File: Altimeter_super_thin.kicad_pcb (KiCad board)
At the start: 4 copper layers, 54.5 x 18 mm, 104 parts, among them IC1 XTSD02GLGEAG, J1 Conn_01x04_Male, J2 Conn_01x02_Male, J3 USB_C_Receptacle_USB2.0, J4 Conn_01x02_Male, Q1 PMV20ENR, U1 150044M155220, U10 MAX77827AEFD+T, U11 SC4215, U2 ESP32-S3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

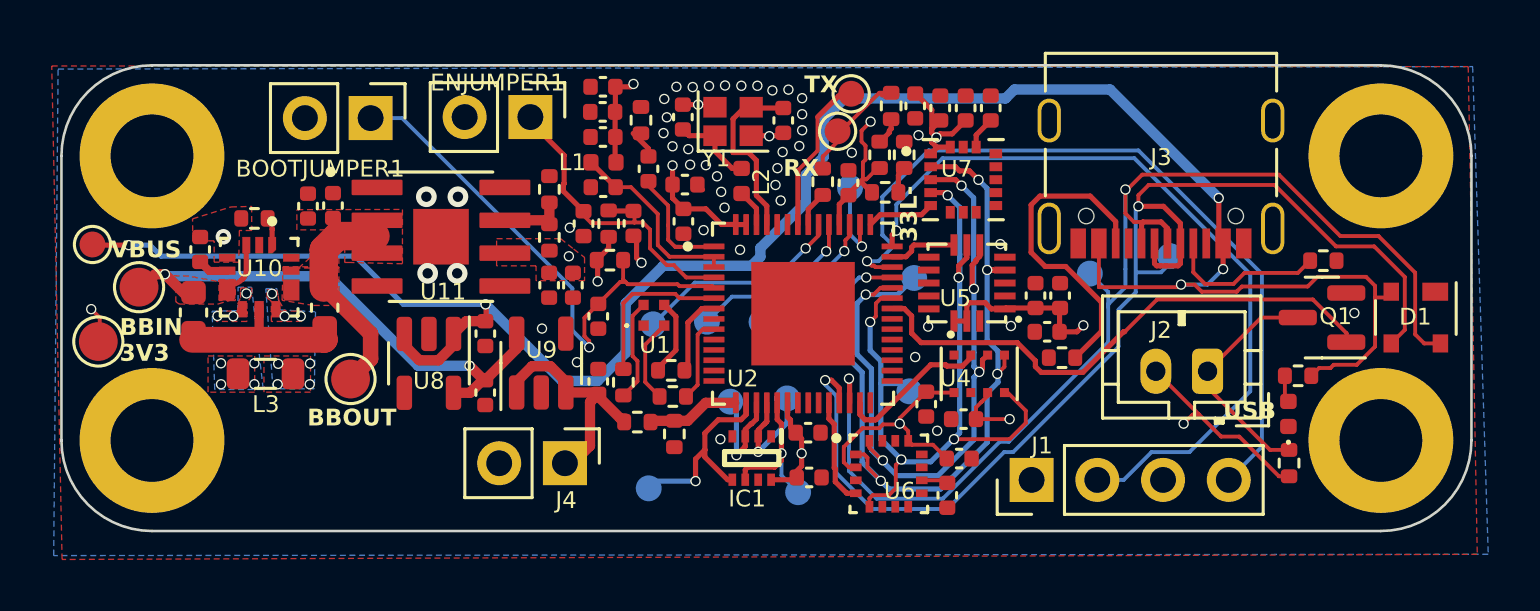
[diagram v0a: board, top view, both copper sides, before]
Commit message: spaced out vias and changed j4
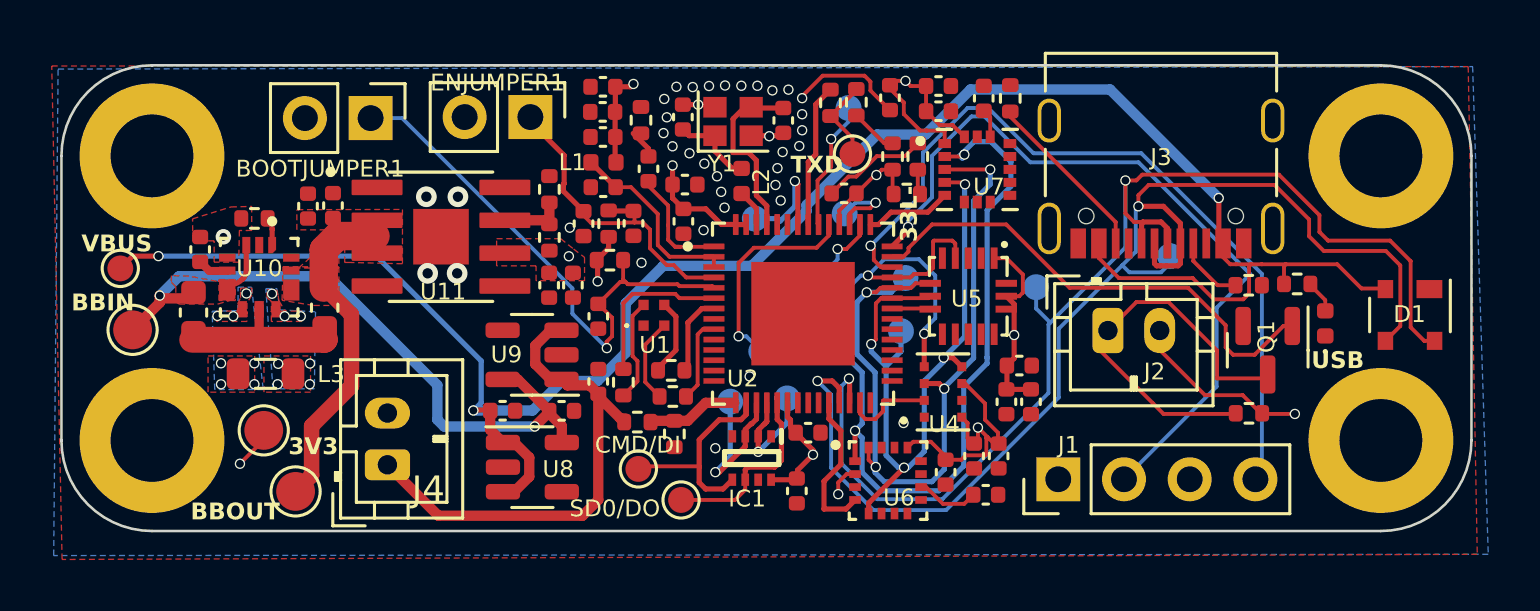
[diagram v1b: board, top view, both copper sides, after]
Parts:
- J4: footprint Connector_PinHeader_2.54mm:PinHeader_1x02_P2.54mm_Vertical -> Connector_JST:JST_PH_B2B-PH-K_1x02_P2.00mm_Vertical
- TP14, TP7: moved to F.Cu
- TP2: moved to B.Cu
- moved TP19 11.3 mm to (113.4, 86.7)
- moved R13 10.2 mm to (119.7, 86.3), turned to -90 degrees
- moved TP9 7.26 mm to (90.8, 99.1), turned to 180 degrees
- moved J4 6.86 mm to (95.6, 100.4), turned to 90 degrees
- moved TP2 6.10 mm to (109.8, 90.9), turned to 180 degrees
- moved U8 5.66 mm to (101.2, 100.5), turned to 0 degrees
- moved TP17 5.29 mm to (113.3, 90.7)
- moved TP8 4.84 mm to (92.0, 101.5)
- moved C39 4.60 mm to (119.5, 98.0), turned to 90 degrees
- moved TP14 4.53 mm to (107.0, 101.8), turned to 0 degrees
- moved J2 4.16 mm to (123.5, 95.2), turned to 0 degrees
- moved C18 4.11 mm to (120.5, 98.0), turned to 90 degrees
- moved TP16 3.95 mm to (112.1, 93.4)
- moved USBLED1 3.78 mm to (131.8, 95.0)
- moved R14 3.55 mm to (130.8, 93.5), turned to 0 degrees
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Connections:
- U2 pad 36: /Buzzer -> /Accel
- U2 pad 41: /IMU/Accelerometer -> /Buzzer
- U5 pad 8: /IMU/Accelerometer -> /Accel
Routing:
- net /SCLK: track 32.0 -> 44.9 mm, vias 5 -> 4
- net Net-(J4-Pin_1): track 9.55 -> 19.7 mm
- net GND: track 10.2 -> 17.5 mm, vias 48 -> 38
- net VBUS: track 84.5 -> 78.4 mm, vias 5 -> 3
- net Net-(J2-Pin_1): track 9.13 -> 15.1 mm
- net Net-(J3-CC2): track 12.6 -> 6.79 mm
- net /power/BBIN: track 22.5 -> 27.7 mm
- net /power/BBOUT: track 8.30 -> 12.9 mm
- net Net-(U2-U0TXD/PROG/GPIO43): track 1.38 -> 5.57 mm
- net /MISO: track 30.9 -> 27.0 mm, vias 5 -> 4
- net Net-(J3-CC1): track 6.19 -> 2.70 mm
- net Net-(U2-MTMS/JTAG/GPIO42): track 8.24 -> 5.02 mm
- net /IMU/Accelerometer: track 2.66 -> 0.00 mm
- net Net-(U2-GPIO21): track 6.17 -> 3.53 mm
- net Net-(U2-MTDO/JTAG/GPIO40): track 5.28 -> 2.97 mm
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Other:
- board text added: "CMD/DI"
- board text added: "RXD"
- board text added: "SD0/DO"
- board text added: "TXD"
- board text removed: "CMD/DI - IC"
- board text removed: "RX"
- board text removed: "SD0/DO - IC"
- board text removed: "TX"

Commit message: initial stage of reitteration
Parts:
- removed C12: 4.2pF, Capacitor_SMD:C_0402_1005Metric
- removed R8: 47.5, Resistor_SMD:R_0402_1005Metric
- C40, TP14, TP7: moved to B.Cu
- IC1: footprint iclr:SOTFL50P160X60-8N -> iclr:SON127P800X600X95-8N; moved to B.Cu
- moved D1 13.2 mm to (122.1, 96.7), turned to 0 degrees
- moved TP15 11.1 mm to (100.5, 101.4)
- moved TP13 10.7 mm to (98.5, 100.6)
- moved USBLED1 10.0 mm to (121.9, 94.5), turned to 180 degrees
- moved R14 9.56 mm to (121.2, 93.5)
- moved R13 7.98 mm to (123.1, 93.5), turned to 0 degrees
- moved TP14 7.09 mm to (105.8, 94.8), turned to 180 degrees
- moved TP3 6.54 mm to (123.2, 98.3)
- moved TP7 6.34 mm to (107.8, 94.8), turned to 180 degrees
- moved Q1 5.43 mm to (134.7, 94.0)
- moved J2 5.28 mm to (128.5, 96.7), turned to 180 degrees
- moved C10 5.10 mm to (103.3, 89.6), turned to 0 degrees
- moved TP4 4.49 mm to (124.4, 96.1)
- moved R10 4.46 mm to (131.5, 94.8), turned to -90 degrees
- moved R5 4.30 mm to (104.4, 93.0), turned to 0 degrees
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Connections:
- U1 pad 1: +3.3V -> +3V3
- U2 pad 1: Net-(U2-LNA_IN/RF) -> unconnected-(U2-LNA_IN/RF-Pad1)
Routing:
- net /Data+: track 46.8 -> 26.4 mm
- net /Data-: track 48.2 -> 29.5 mm
- net Net-(IC1-SD3/CS): track 4.69 -> 13.0 mm
- net Net-(IC1-CLK): track 6.41 -> 14.5 mm
- net Net-(J4-Pin_1): track 19.7 -> 13.7 mm
- net Net-(IC1-SD0/DO): track 7.26 -> 13.0 mm, vias 0 -> 1
- net Net-(J3-CC2): track 6.79 -> 1.66 mm
- net Net-(J2-Pin_1): track 15.1 -> 10.4 mm
- net GND: track 17.5 -> 12.8 mm, vias 38 -> 36
- net Net-(U2-LNA_IN/RF): track 4.61 -> 0.00 mm
- net VBUS: track 78.4 -> 73.9 mm
- net /Buzzer: track 19.1 -> 23.5 mm
- net /BOOT: track 21.2 -> 17.1 mm
- net Net-(J3-CC1): track 2.70 -> 5.40 mm
- net Net-(U2-GPIO1/ADC1_CH0): track 6.27 -> 3.74 mm
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
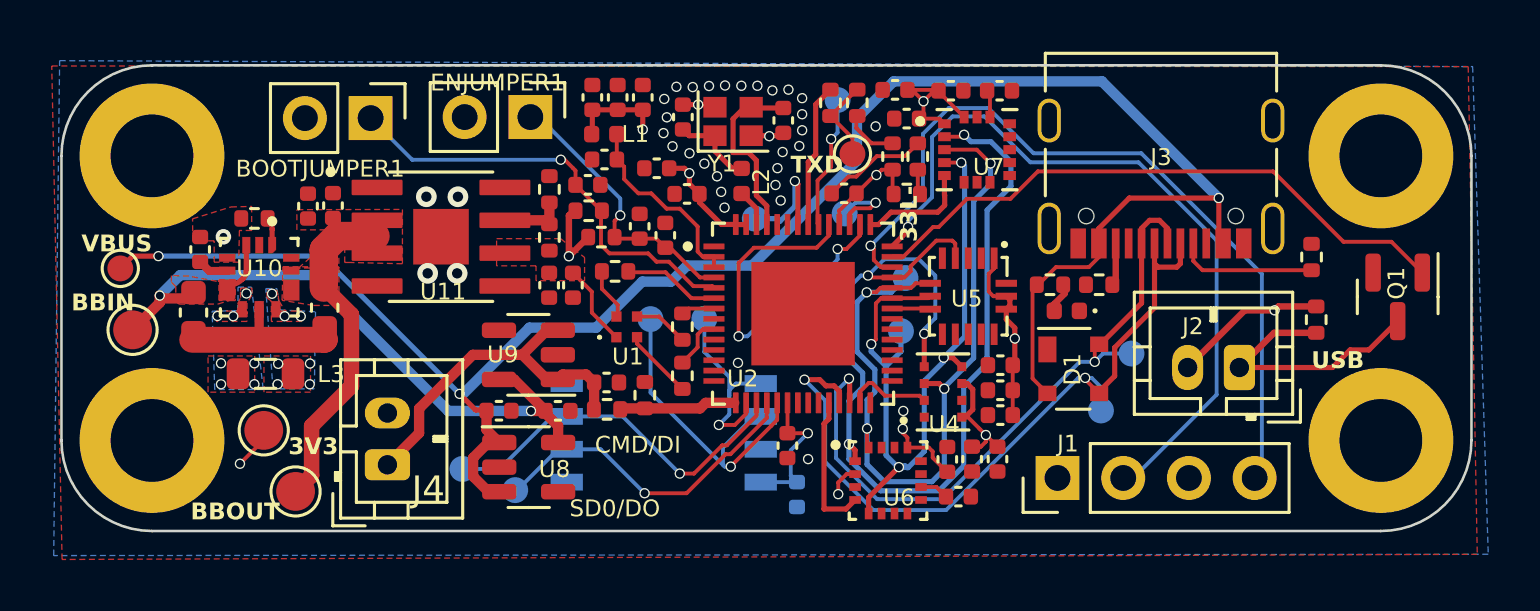
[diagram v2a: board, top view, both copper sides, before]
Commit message: rerouted spi bus and changed NAND
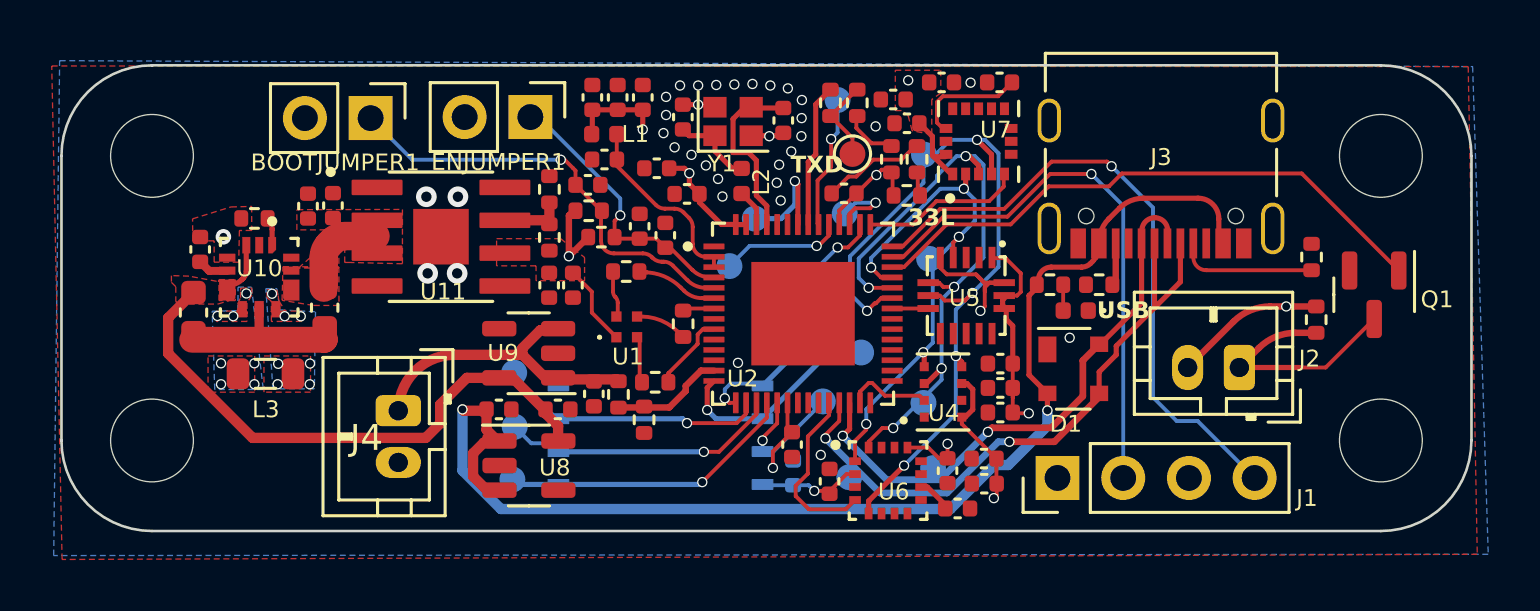
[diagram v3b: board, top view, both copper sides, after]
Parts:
- removed IC1: XTSD02GLGEAG, iclr:SON127P800X600X95-8N
- removed TP5: TestPoint, TestPoint:TestPoint_Pad_D1.0mm
- removed TP6, TP8, TP9: TestPoint, TestPoint:TestPoint_Pad_D1.5mm
- added C12: 1uF, Capacitor_SMD:C_0402_1005Metric, F.Cu at (112.7, 101.1)
- added IC2: AS5F32G04SNDA-08LIN, iclr:SON127P600X800X65-8N, B.Cu at (106.2, 99.3)
- added TP20: TestPoint, TestPoint:TestPoint_Pad_D1.0mm, B.Cu at (100.4, 101.0)
- added TP21: TestPoint, TestPoint:TestPoint_Pad_D1.0mm, B.Cu at (112.4, 98.0)
- H1, H2, H3, H4: footprint MountingHole:MountingHole_3.2mm_M3_DIN965_Pad -> MountingHole:MountingHole_3.2mm_M3_DIN965
- moved TP3 10.1 mm to (113.5, 100.9)
- moved TP4 8.86 mm to (116.7, 100.6)
- moved TP14 8.24 mm to (113.9, 96.1)
- moved TP12 6.88 mm to (116.3, 88.5)
- moved TP11 5.54 mm to (116.5, 92.5)
- moved TP10 4.88 mm to (116.3, 98.0)
- moved TP13 4.22 mm to (100.5, 96.9)
- moved TP7 3.86 mm to (111.7, 95.4)
- moved TP15 2.45 mm to (100.5, 99.0)
- moved TP18 2.44 mm to (108.8, 92.8)
- moved C22 2.26 mm to (115.2, 86.3), turned to 180 degrees
- moved J4 2.13 mm to (96.0, 98.3), turned to -90 degrees
- moved G*** 2.10 mm to (92.4, 94.8)
- moved C23 1.82 mm to (117.0, 85.7), turned to 0 degrees
- moved R7 1.08 mm to (106.0, 97.2), turned to 0 degrees
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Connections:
- C40 pad 1: +3V3 -> GND
- C40 pad 2: GND -> +3V3
- TP13 pad 1: Net-(IC1-CLK) -> Net-(IC2-WP#/SIO2)
- TP14 pad 1: Net-(IC1-SD0/DO) -> Net-(IC2-SCLK)
- TP15 pad 1: Net-(IC1-SD3/CS) -> Net-(IC2-SO/SIO1)
- TP7 pad 1: Net-(IC1-CMD/DI) -> Net-(IC2-SI/SIO0)
- U2 pad 13: unconnected-(U2-GPIO8/ADC1_CH7-Pad13) -> /BattVolt
- U2 pad 14: unconnected-(U2-GPIO9/ADC1_CH8-Pad14) -> Net-(IC2-SCLK)
- U2 pad 15: /BattVolt -> Net-(IC2-SI/SIO0)
- U2 pad 16: Net-(IC1-CMD/DI) -> Net-(IC2-WP#/SIO2)
- U2 pad 17: Net-(IC1-CLK) -> Net-(IC2-SO/SIO1)
- U2 pad 18: Net-(IC1-SD3/CS) -> Net-(IC2-CS#)
- U2 pad 19: Net-(IC1-SD0/DO) -> Net-(IC2-HOLD#/SIO3)
- U2 pad 40: Net-(J1-Pin_4) -> /Buzzer
- U2 pad 41: /Buzzer -> Net-(J1-Pin_2)
- U2 pad 42: Net-(J1-Pin_2) -> Net-(J1-Pin_4)
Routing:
- net VBUS: track 73.9 -> 49.2 mm, vias 3 -> 2
- net /SCLK: track 43.8 -> 20.9 mm, vias 4 -> 5
- net Net-(IC1-CLK): track 14.5 -> 0.00 mm, vias 1 -> 0
- net Net-(IC1-SD3/CS): track 13.0 -> 0.00 mm, vias 1 -> 0
- net Net-(IC1-SD0/DO): track 13.0 -> 0.00 mm, vias 1 -> 0
- net Net-(IC2-CS#): track 0.00 -> 11.7 mm, vias 0 -> 1
- net Net-(IC2-SO/SIO1): track 0.00 -> 10.8 mm, vias 0 -> 1
- net Net-(IC2-WP#/SIO2): track 0.00 -> 10.4 mm, vias 0 -> 1
- net /power/BBOUT: track 12.9 -> 3.64 mm
- net Net-(IC2-SCLK): track 0.00 -> 8.38 mm, vias 0 -> 1
- net Net-(IC1-CMD/DI): track 7.87 -> 0.00 mm, vias 1 -> 0
- net Net-(J1-Pin_2): track 29.1 -> 21.3 mm
- net /MOSI: track 31.2 -> 24.9 mm, vias 4 -> 5
- net Net-(J1-Pin_4): track 30.8 -> 24.7 mm
- net GND: track 12.8 -> 18.6 mm, vias 36 -> 35
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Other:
- board text added: "33L"
- board text added: "CLK"
- board text added: "CS"
- board text added: "SIO0"
- board text added: "SIO1"
- board text added: "SIO3"
- board text added: "WP"
- board text added: "Артёмитер"
- board text removed: "33L-"
- board text removed: "3V3"
- board text removed: "BBIN"
- board text removed: "BBOUT"
- board text removed: "CLK - IC"
- board text removed: "CMD/DI"
- board text removed: "Cert. Stargazer"
- board text removed: "SD0/DO"
- board text removed: "SD3/CS - IC"
- board text removed: "VBUS"

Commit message: fixed courtyard overlap in one place
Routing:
- net GND: vias 35 -> 36
